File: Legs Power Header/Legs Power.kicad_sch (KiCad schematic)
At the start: 25 parts, among them J10 Conn_01x04_Pin, J11 Conn_01x04_Pin, J12 Conn_01x04_Pin, J13 Conn_01x04_Pin, J14 Conn_01x04_Pin, J15 Conn_01x04_Pin, J16 Conn_01x04_Pin, J17 Conn_01x04_Pin, J18 Conn_01x04_Pin, J19 Conn_01x04_Pin, J2 Conn_01x04_Pin, J20 Conn_01x04_Pin, J21 Conn_01x04_Pin, J22 Conn_01x04_Pin, J23 Conn_01x04_Pin, J24 Conn_01x04_Pin, J25 Conn_01x04_Pin, J26 Conn_01x04_Pin, J3 Conn_01x04_Pin, J4 Conn_01x04_Pin, J5 Conn_01x04_Pin, J7 Conn_01x04_Pin, J8 Conn_01x04_Pin, J9 Conn_01x04_Pin

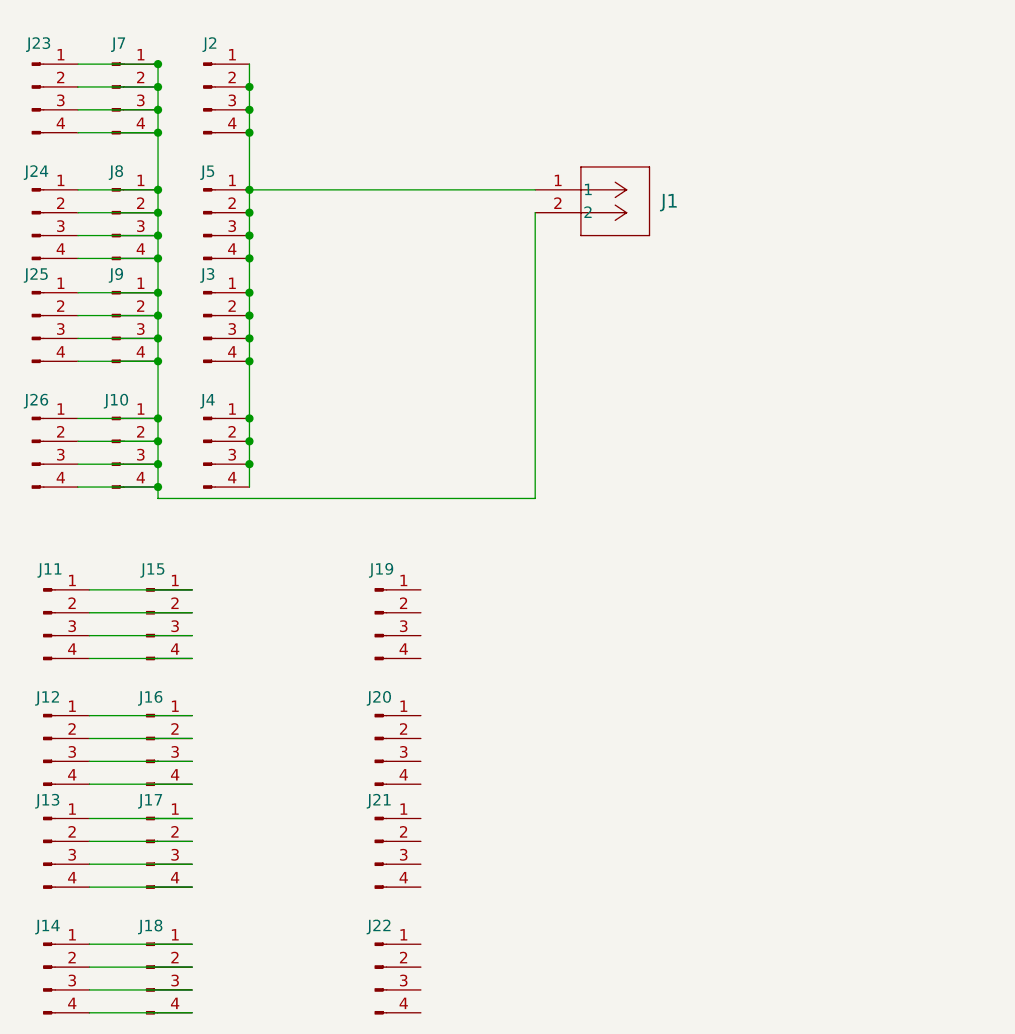
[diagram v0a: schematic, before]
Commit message: Completed Basic Header Board for Power With Power Supply
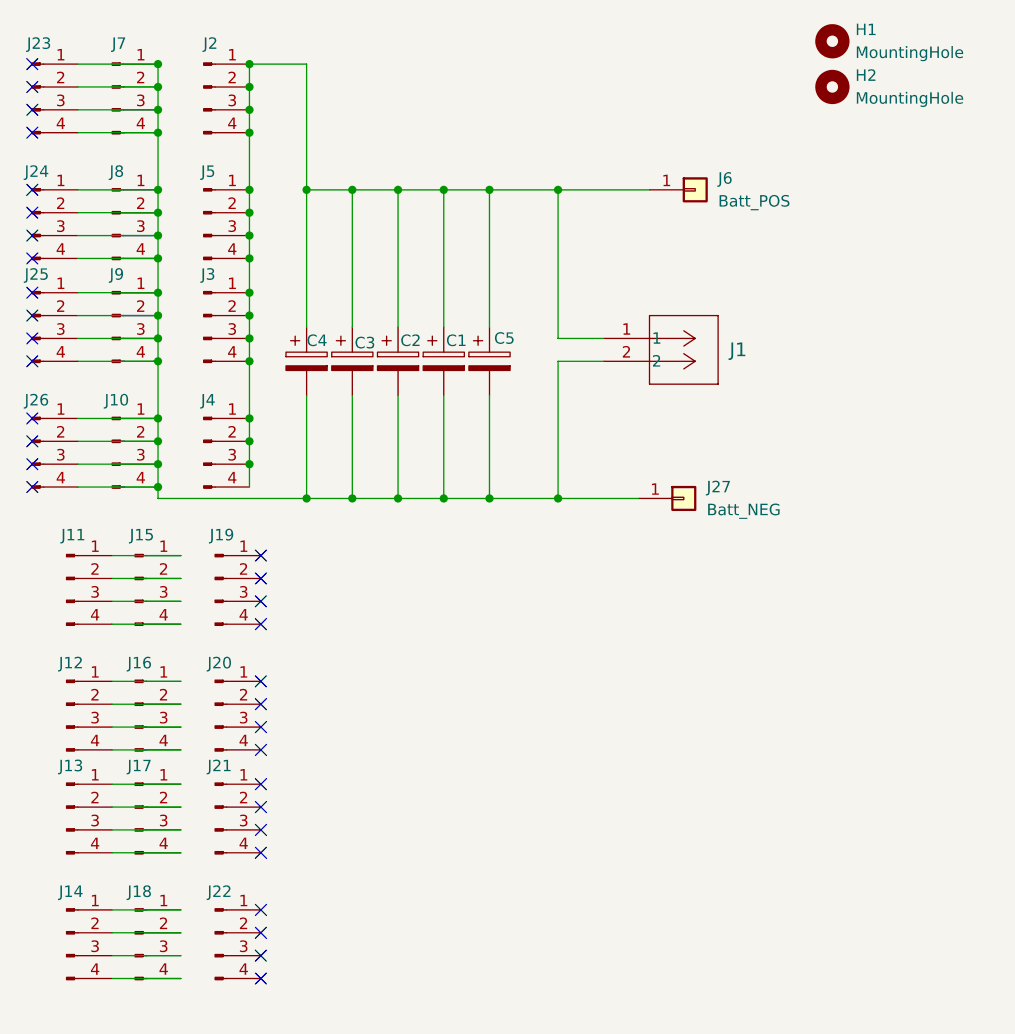
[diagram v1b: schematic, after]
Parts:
- added C1, C2, C3, C4, C5: C_Polarized, Capacitor_THT:CP_Radial_D12.5mm_P5.00mm, symbol Device:C_Polarized
- added H1, H2: MountingHole, MountingHole:MountingHole_3.2mm_M3, symbol Mechanical:MountingHole
- added J27: Batt_NEG, Connector_Wire:SolderWirePad_1x01_SMD_5x10mm, symbol Connector_Generic:Conn_01x01
- added J6: Batt_POS, Connector_Wire:SolderWirePad_1x01_SMD_5x10mm, symbol Connector_Generic:Conn_01x01
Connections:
- net at J1.2, J10.1 (Pin_1), J10.2 (Pin_2)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: now also C1.2, C2.2, C3.2, C4.2, C5.2, J27.1 (Pin_1)
- net at J1.1, J2.1 (Pin_1), J2.2 (Pin_2)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: now also C1.1, C2.1, C3.1, C4.1, C5.1, J6.1 (Pin_1)
- no-connect marks 0 -> 32
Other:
- moved on the sheet: J1, J11, J12, J13, J14, J15, J16, J17, J18, J19, J20, J21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
